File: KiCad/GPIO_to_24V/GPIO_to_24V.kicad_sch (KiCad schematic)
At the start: 5 parts, among them U1 ! 4N33 !, U1 TLP627-4

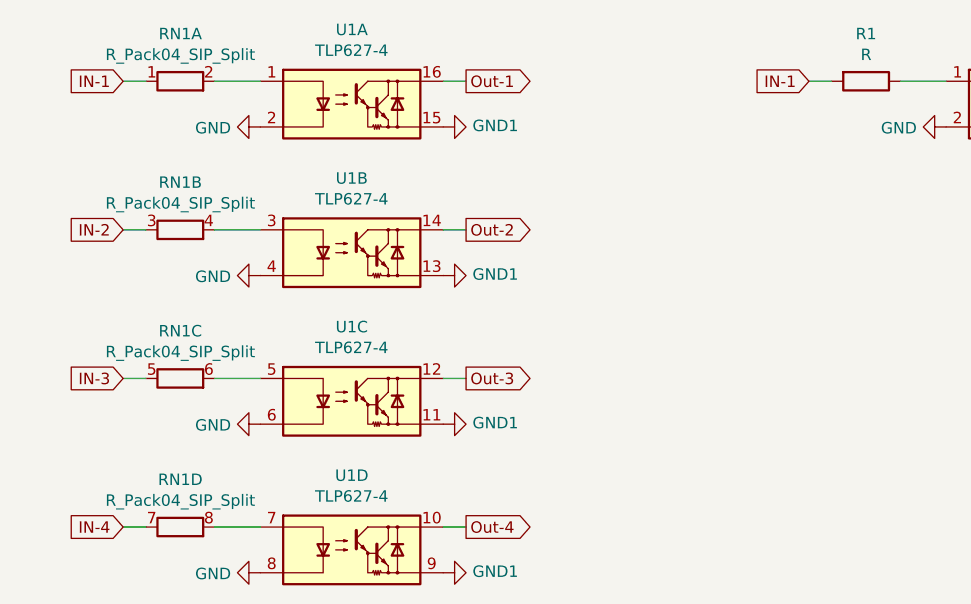
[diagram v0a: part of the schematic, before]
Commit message: schematics update
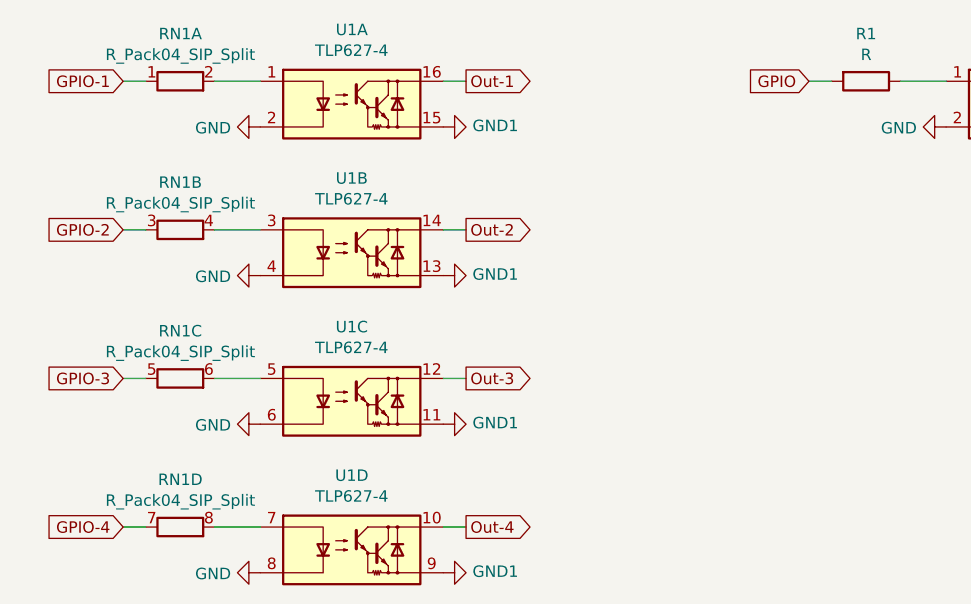
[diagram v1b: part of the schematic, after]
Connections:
- net IN-1 renamed GPIO
- net GPIO: no longer RN1.1 (R1.1)
- net IN-2 renamed GPIO-2
- net IN-3 renamed GPIO-3
- net IN-4 renamed GPIO-4
- new net GPIO-1: RN1.1 (R1.1)
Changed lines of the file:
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@@
     )
   )
-  (global_label "IN-4" (shape input) (at 46.99 80.01 180)
+  (global_label "GPIO-4" (shape input) (at 46.99 80.01 180)
     (effects (font (size 1.27 1.27)) (justify right))
     (property "Intersheetrefs" "${INTERSHEET_REFS}" (at 46.99 80.01 0)
@@
     )
   )
-  (global_label "IN-3" (shape input) (at 46.99 63.5 180)
+  (global_label "GPIO-3" (shape input) (at 46.99 63.5 180)
     (effects (font (size 1.27 1.27)) (justify right))
     (property "Intersheetrefs" "${INTERSHEET_REFS}" (at 46.99 63.5 0)
@@
     )
   )
-  (global_label "IN-1" (shape input) (at 46.99 30.48 180)
+  (global_label "GPIO-1" (shape input) (at 46.99 30.48 180)
     (effects (font (size 1.27 1.27)) (justify right))
     (property "Intersheetrefs" "${INTERSHEET_REFS}" (at 46.99 30.48 0)
@@
     )
   )
-  (global_label "IN-1" (shape input) (at 123.19 30.48 180)
+  (global_label "GPIO" (shape input) (at 123.19 30.48 180)
     (effects (font (size 1.27 1.27)) (justify right))
     (property "Intersheetrefs" "${INTERSHEET_REFS}" (at 123.19 30.48 0)
@@
     )
   )
-  (global_label "IN-2" (shape input) (at 46.99 46.99 180)
+  (global_label "GPIO-2" (shape input) (at 46.99 46.99 180)
     (effects (font (size 1.27 1.27)) (justify right))
     (property "Intersheetrefs" "${INTERSHEET_REFS}" (at 46.99 46.99 0)

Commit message: KiCad stuff...
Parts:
- removed unit 2 of RN1
- removed unit 3 of RN1
- removed unit 4 of RN1
- removed unit 2 of U1
- removed unit 3 of U1
- removed unit 4 of U1
- added RN2: 1.8k, Resistor_THT:R_Array_SIP8, symbol Device:R_Pack04_SIP_Split
- added RN3: 3.3k, Resistor_THT:R_Array_SIP5, symbol Device:R_Network04_Split
- added RN4: 10k, Resistor_THT:R_Array_SIP8, symbol Device:R_Pack04_SIP_Split
- added U2: 2501-4, Package_DIP:DIP-16_W7.62mm, symbol Isolator:PC847
- added U3: ULN2803A, symbol Transistor_Array:ULN2803A
- R1: value R -> 1k
- RN1: value R_Pack04_SIP_Split -> 1.5k
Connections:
- net GND: now also U2.2
- net GND1: now also RN3.1 (R1), U3.9 (GND)
- net GPIO-1: now also RN2.2 (R1.2)
- net Out-1: now also RN3.2 (R1.2), U2.15, U3.18 (O1)
- new net: RN2.1 (R1.1), U2.1
- new net: RN4.1 (R1.1), U3.1 (I1)
- new net +24V: U2.16, U3.10 (COM)
- new net In-1: RN4.2 (R1.2)
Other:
- moved on the sheet: D?, R1, U1
